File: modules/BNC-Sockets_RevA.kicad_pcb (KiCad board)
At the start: 2 copper layers, 3 parts

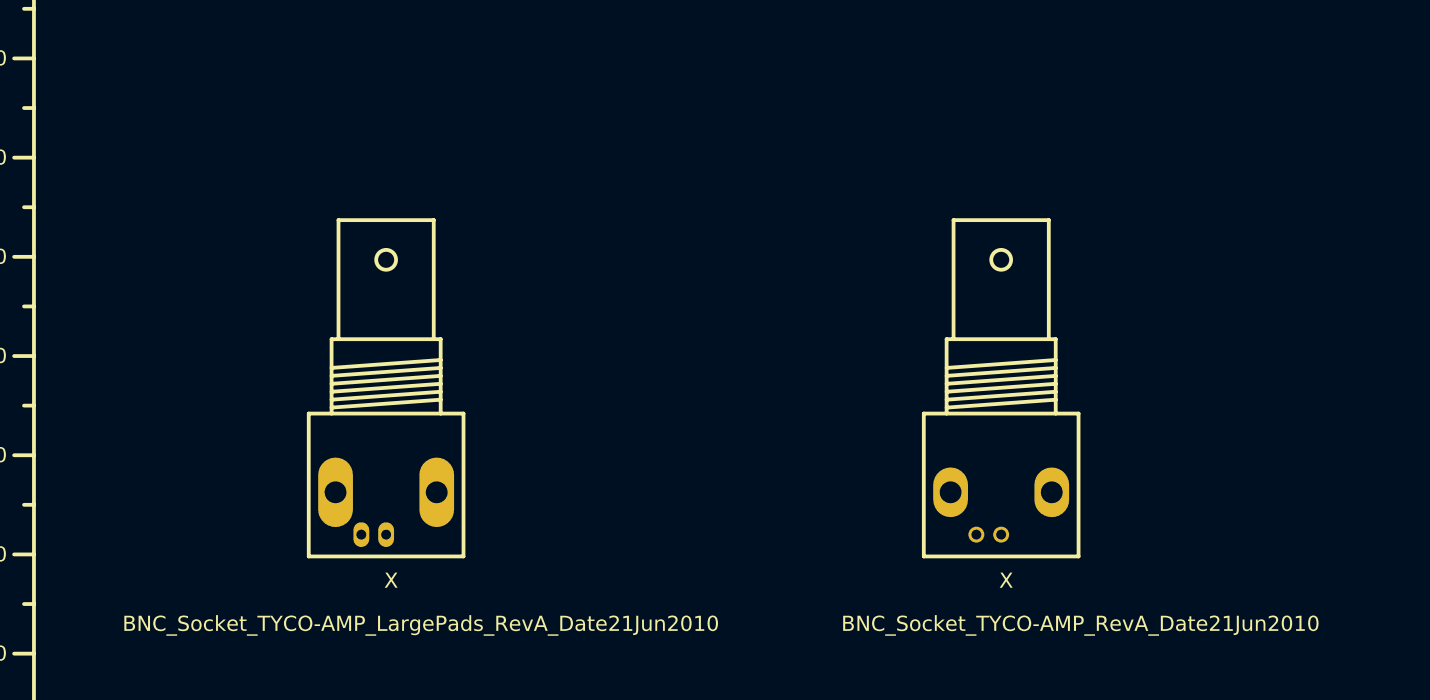
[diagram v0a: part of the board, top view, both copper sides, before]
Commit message: Some new 3D models (7-Segment and BNC-socket) and some lost(???)  .mod files
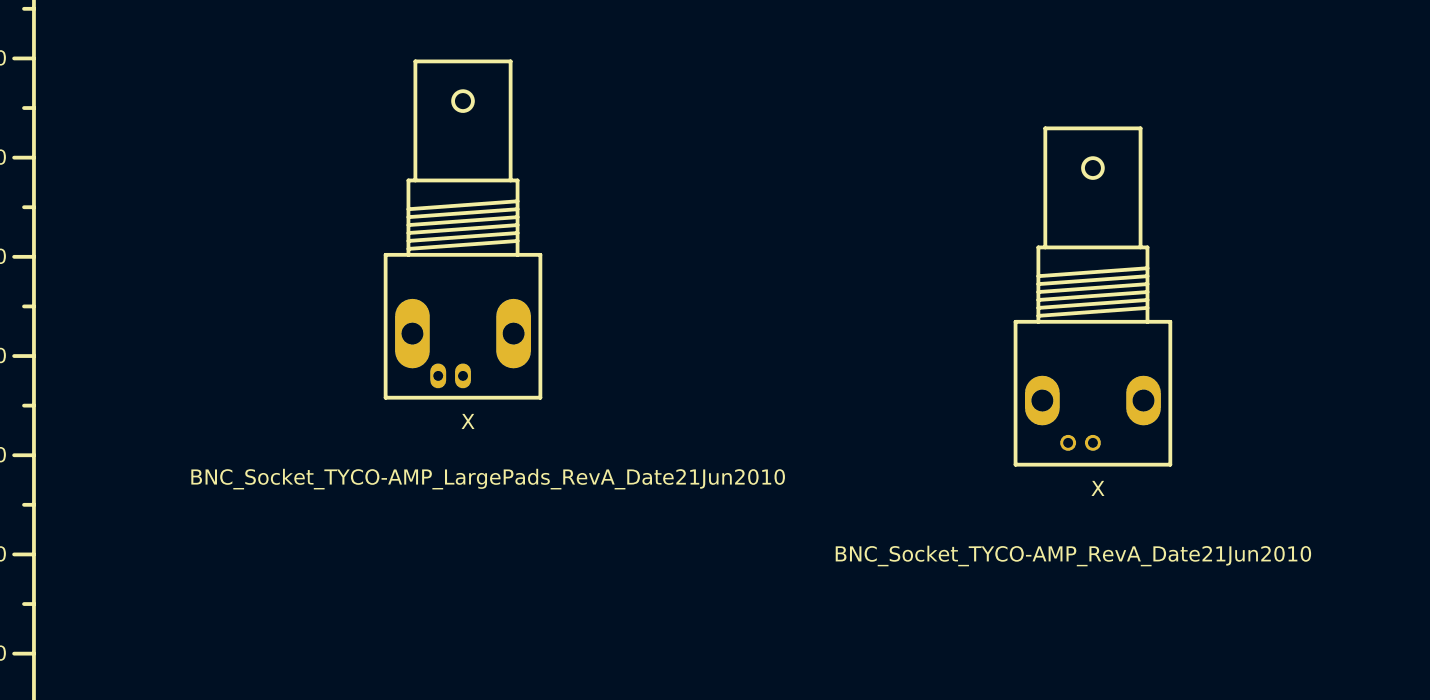
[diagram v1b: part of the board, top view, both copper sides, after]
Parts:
- moved X 17.8 mm to (179.2, 69.5)
- moved X 13.1 mm to (242.8, 76.2)
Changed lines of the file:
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@@
     (links 0)
     (no_connects 0)
-    (area 13.77313 22.055699 274.079733 179.10071)
+    (area 13.77313 5.6024 274.079733 179.10071)
     (thickness 1.6002)
     (drawings 6)
@@
     (fp_line (start 9.99998 0) (end 9.99998 1.99898) (layer F.SilkS) (width 0.381))
   )
-  (module BNC_Socket_TYCO-AMP_LargePads_RevA_Date21Jun2010 (layer Vorderseite)
-    (at 171.5 85.5)
+  (module BNC_Socket_TYCO-AMP_RevA_Date21Jun2010 (layer Vorderseite)
+    (at 242.75 76.25)
     (descr "BNC Socket TYCO AMP")
     (tags "BNC Socket TYCO AMP")
@@
       (effects (font (size 1.524 1.524) (thickness 0.3048)))
     )
-    (fp_text value BNC_Socket_TYCO-AMP_LargePads_RevA_Date21Jun2010 (at 3.5 14) (layer F.SilkS)
+    (fp_text value BNC_Socket_TYCO-AMP_RevA_Date21Jun2010 (at -2 16.25) (layer F.SilkS)
+      (effects (font (size 1.524 1.524) (thickness 0.3048)))
+    )
+    (fp_line (start -5.4991 -11.80084) (end 5.4991 -12.60094) (layer F.SilkS) (width 0.381))
+    (fp_line (start -5.4991 -11.00074) (end 5.4991 -11.80084) (layer F.SilkS) (width 0.381))
+    (fp_line (start -5.4991 -10.20064) (end 5.4991 -11.00074) (layer F.SilkS) (width 0.381))
+    (fp_line (start -5.4991 -9.40054) (end 5.4991 -10.20064) (layer F.SilkS) (width 0.381))
+    (fp_line (start -5.4991 -8.60044) (end 5.4991 -9.40054) (layer F.SilkS) (width 0.381))
+    (fp_line (start -5.4991 -7.80034) (end 5.4991 -8.60044) (layer F.SilkS) (width 0.381))
+    (fp_circle (center 0 -22.69998) (end 1.00076 -22.69998) (layer F.SilkS) (width 0.381))
+    (fp_line (start 4.8006 -14.69898) (end 4.8006 -26.70048) (layer F.SilkS) (width 0.381))
+    (fp_line (start 4.8006 -26.70048) (end -4.8006 -26.70048) (layer F.SilkS) (width 0.381))
+    (fp_line (start -4.8006 -26.70048) (end -4.8006 -14.69898) (layer F.SilkS) (width 0.381))
+    (fp_line (start 5.4991 -7.2009) (end 5.4991 -14.69898) (layer F.SilkS) (width 0.381))
+    (fp_line (start 5.4991 -14.69898) (end -5.4991 -14.69898) (layer F.SilkS) (width 0.381))
+    (fp_line (start -5.4991 -14.69898) (end -5.4991 -7.2009) (layer F.SilkS) (width 0.381))
+    (fp_line (start -7.80034 7.2009) (end 7.80034 7.2009) (layer F.SilkS) (width 0.381))
+    (fp_line (start 7.80034 7.2009) (end 7.80034 -7.2009) (layer F.SilkS) (width 0.381))
+    (fp_line (start 7.80034 -7.2009) (end -7.80034 -7.2009) (layer F.SilkS) (width 0.381))
+    (fp_line (start -7.80034 -7.2009) (end -7.80034 7.2009) (layer F.SilkS) (width 0.381))
+    (pad 2 thru_hole oval (at -5.09778 0.7366) (size 3.50012 5.00126) (drill 2.19964)
+      (layers *.Cu *.Mask F.SilkS)
+    )
+    (pad 2 thru_hole oval (at 5.10032 0.7366) (size 3.50012 5.00126) (drill 2.19964)
+      (layers *.Cu *.Mask F.SilkS)
+    )
+    (pad 1 thru_hole circle (at 0 5.00126) (size 1.6002 1.6002) (drill 1.00076)
+      (layers *.Cu *.Mask F.SilkS)
+    )
+    (pad 2 thru_hole circle (at -2.49936 5.00126) (size 1.6002 1.6002) (drill 1.00076)
+      (layers *.Cu *.Mask F.SilkS)
+    )
+    (model BNC-Socket_Wings3D_RevA_22Sep2013/BNC-Socket_RevA_Faktor03937_22Sep2013.wrl
+      (at (xyz 0 0 0))
+      (scale (xyz 0.3937 0.3937 0.3937))
+      (rotate (xyz 0 0 0))
+    )
+  )
+  (module BNC_Socket_TYCO-AMP_LargePads_RevA_Date21Jun2010 (layer Vorderseite)
+    (at 179.25 69.5)
+    (descr "BNC Socket TYCO AMP")
+    (tags "BNC Socket TYCO AMP")
+    (fp_text reference X (at 0.508 9.652) (layer F.SilkS)
+      (effects (font (size 1.524 1.524) (thickness 0.3048)))
+    )
+    (fp_text value BNC_Socket_TYCO-AMP_LargePads_RevA_Date21Jun2010 (at 2.5 15.25) (layer F.SilkS)
       (effects (font (size 1.524 1.524) (thickness 0.3048)))
     )
@@
       (layers *.Cu *.Mask F.SilkS)
     )
-  )
-  (module BNC_Socket_TYCO-AMP_RevA_Date21Jun2010 (layer Vorderseite)
-    (at 233.5 85.5)
-    (descr "BNC Socket TYCO AMP")
-    (tags "BNC Socket TYCO AMP")
-    (fp_text reference X (at 0.508 9.652) (layer F.SilkS)
-      (effects (font (size 1.524 1.524) (thickness 0.3048)))
-    )
-    (fp_text value BNC_Socket_TYCO-AMP_RevA_Date21Jun2010 (at 8 14) (layer F.SilkS)
-      (effects (font (size 1.524 1.524) (thickness 0.3048)))
-    )
-    (fp_line (start -5.4991 -11.80084) (end 5.4991 -12.60094) (layer F.SilkS) (width 0.381))
-    (fp_line (start -5.4991 -11.00074) (end 5.4991 -11.80084) (layer F.SilkS) (width 0.381))
-    (fp_line (start -5.4991 -10.20064) (end 5.4991 -11.00074) (layer F.SilkS) (width 0.381))
-    (fp_line (start -5.4991 -9.40054) (end 5.4991 -10.20064) (layer F.SilkS) (width 0.381))
-    (fp_line (start -5.4991 -8.60044) (end 5.4991 -9.40054) (layer F.SilkS) (width 0.381))
-    (fp_line (start -5.4991 -7.80034) (end 5.4991 -8.60044) (layer F.SilkS) (width 0.381))
-    (fp_circle (center 0 -22.69998) (end 1.00076 -22.69998) (layer F.SilkS) (width 0.381))
-    (fp_line (start 4.8006 -14.69898) (end 4.8006 -26.70048) (layer F.SilkS) (width 0.381))
-    (fp_line (start 4.8006 -26.70048) (end -4.8006 -26.70048) (layer F.SilkS) (width 0.381))
-    (fp_line (start -4.8006 -26.70048) (end -4.8006 -14.69898) (layer F.SilkS) (width 0.381))
-    (fp_line (start 5.4991 -7.2009) (end 5.4991 -14.69898) (layer F.SilkS) (width 0.381))
-    (fp_line (start 5.4991 -14.69898) (end -5.4991 -14.69898) (layer F.SilkS) (width 0.381))
-    (fp_line (start -5.4991 -14.69898) (end -5.4991 -7.2009) (layer F.SilkS) (width 0.381))
-    (fp_line (start -7.80034 7.2009) (end 7.80034 7.2009) (layer F.SilkS) (width 0.381))
-    (fp_line (start 7.80034 7.2009) (end 7.80034 -7.2009) (layer F.SilkS) (width 0.381))
-    (fp_line (start 7.80034 -7.2009) (end -7.80034 -7.2009) (layer F.SilkS) (width 0.381))
-    (fp_line (start -7.80034 -7.2009) (end -7.80034 7.2009) (layer F.SilkS) (width 0.381))
-    (pad 2 thru_hole oval (at -5.09778 0.7366) (size 3.50012 5.00126) (drill 2.19964)
-      (layers *.Cu *.Mask F.SilkS)
-    )
-    (pad 2 thru_hole oval (at 5.10032 0.7366) (size 3.50012 5.00126) (drill 2.19964)
-      (layers *.Cu *.Mask F.SilkS)
-    )
-    (pad 1 thru_hole circle (at 0 5.00126) (size 1.6002 1.6002) (drill 1.00076)
-      (layers *.Cu *.Mask F.SilkS)
-    )
-    (pad 2 thru_hole circle (at -2.49936 5.00126) (size 1.6002 1.6002) (drill 1.00076)
-      (layers *.Cu *.Mask F.SilkS)
-    )
-  )
+    (model BNC-Socket_Wings3D_RevA_22Sep2013/BNC-Socket_RevA_Faktor03937_22Sep2013.wrl
+      (at (xyz 0 0 0))
+      (scale (xyz 0.3937 0.3937 0.3937))
+      (rotate (xyz 0 0 0))
+    )
+  )

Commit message: Updates for pretty folders.
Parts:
- added Sym: Symbol_CreativeCommonsPublicDomain_SilkScreenTop_Small, Symbols:Symbol_CreativeCommonsPublicDomain_SilkScreenTop_Small, F.Cu at (74.0, 180.5)
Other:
- board text added: "BNC-Sockets_RevA.pretty (was BNC-Sockets_RevA.mod)"
- board text added: "KiCAD Footprints of some BNC-Sockets from the folder"
- board text removed: "BNC-Sockets_RevA.mod"
- board text removed: "KiCAD Footprints of some BNC-Sockets from the file"
